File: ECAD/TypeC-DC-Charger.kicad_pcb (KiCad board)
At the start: 2 copper layers, 3 parts, among them U1 LM5175RHF, U2 TPS25741

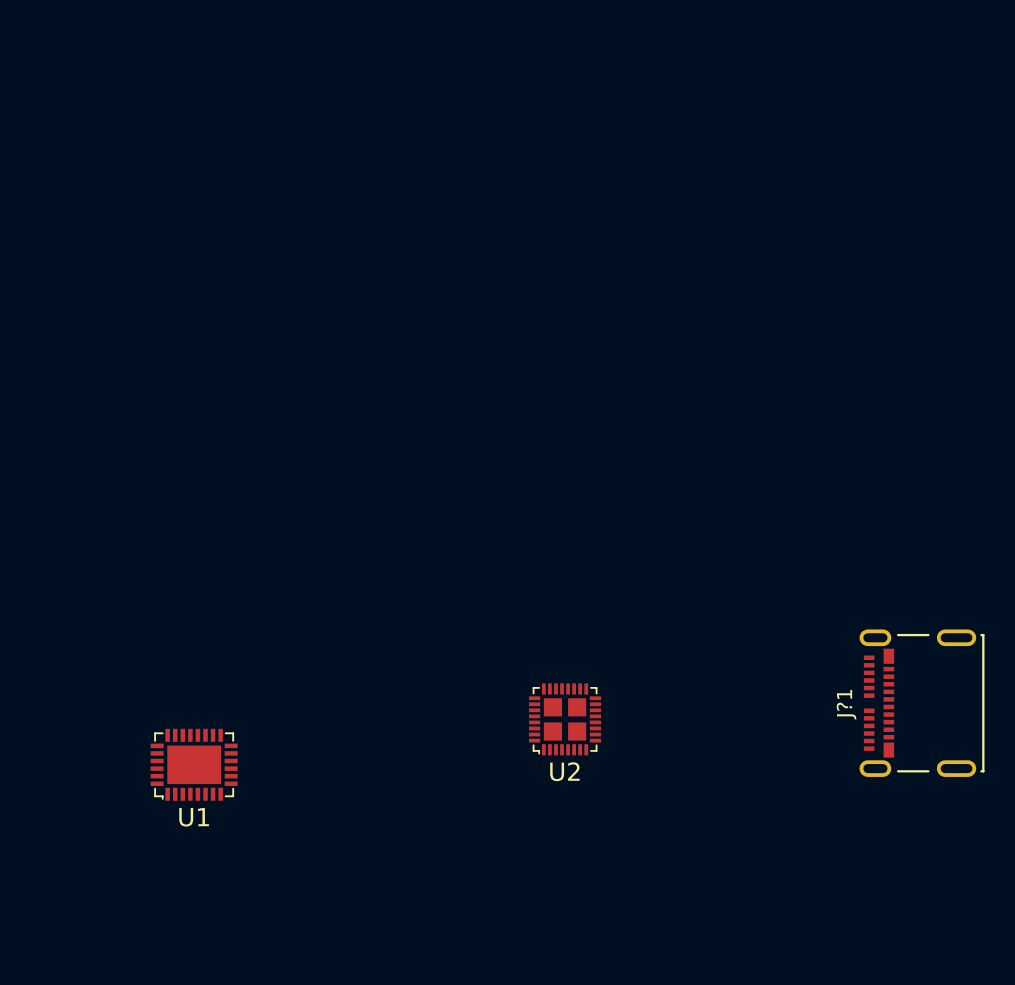
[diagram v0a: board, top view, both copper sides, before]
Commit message: Soft start circuit, Switched BC1.2 IC, more 0402 parts now, placement and routing.
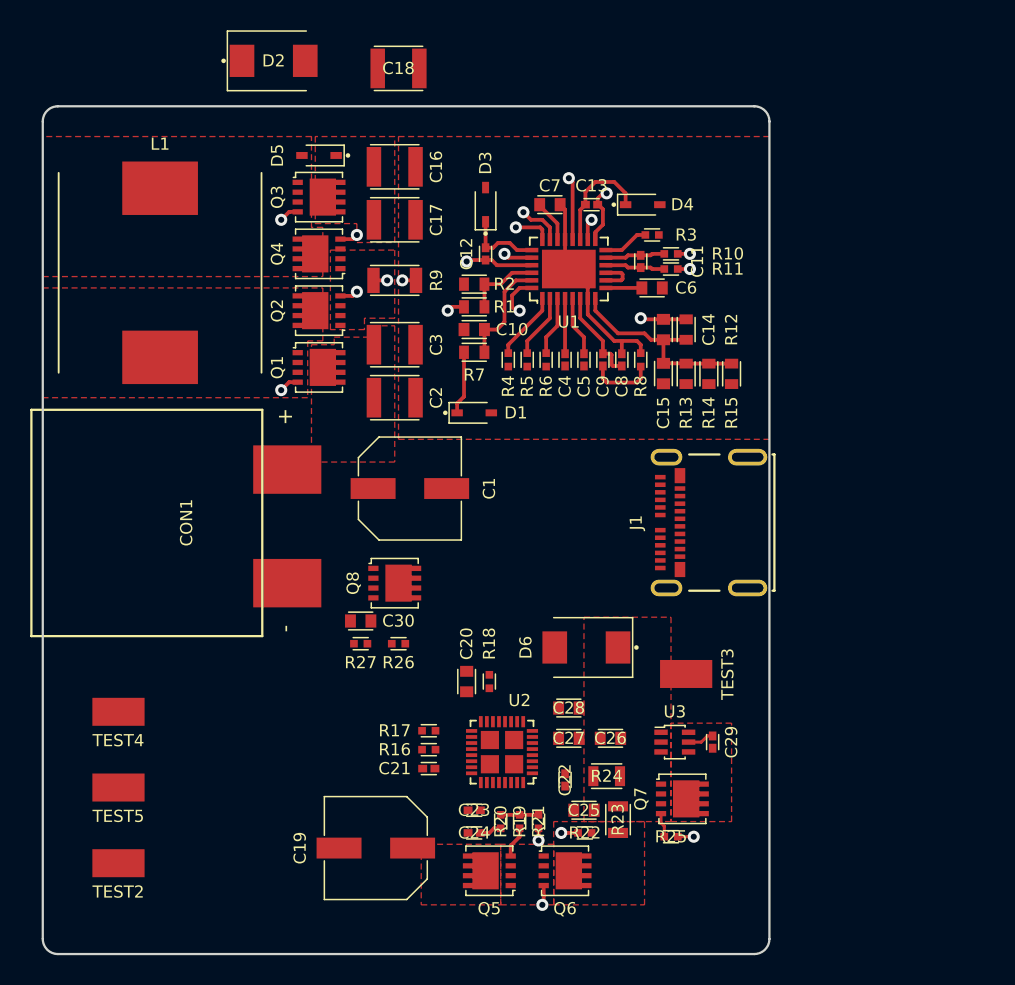
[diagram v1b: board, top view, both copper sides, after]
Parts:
- removed J?1: USB_C_SOCKET_RA_SMD, Applidyne_USB:MOLEX-105450-0101
- added C1: 100UF_ELEC_35V_660X580M, Applidyne_Capacitor:CAPAE660X580DD180L260L, F.Cu at (124.2, 75.2)
- added C10: 100NF_X7R_1608M, Applidyne_Capacitor:CAPC1608X90L, F.Cu at (128.5, 64.8)
- added C11: 47PF_X7R_1005M, Applidyne_Capacitor:CAPC1005X60L, F.Cu at (139.5, 60.2)
- added C12: 100NF_X7R_1005M, Applidyne_Capacitor:CAPC1005X60L, F.Cu at (129.2, 59.8)
- added C13: 100NF_X7R_1005M, Applidyne_Capacitor:CAPC1005X60L, F.Cu at (136.2, 56.5)
- added C14: 22NF_X7R_1608M, Applidyne_Capacitor:CAPC1608X90L, F.Cu at (141.0, 64.8)
- added C15: 100NF_X7R_1608M, Applidyne_Capacitor:CAPC1608X90L, F.Cu at (141.0, 67.7)
- added C16: 22UF_X7R_3225M, Applidyne_Capacitor:CAPC3225X170L, F.Cu at (123.2, 54.0)
- added C17: 22UF_X7R_3225M, Applidyne_Capacitor:CAPC3225X170L, F.Cu at (123.2, 57.5)
- added C18: 22UF_X7R_3225M, Applidyne_Capacitor:CAPC3225X170L, F.Cu at (123.5, 47.5)
- added C19: 100UF_ELEC_35V_660X580M, Applidyne_Capacitor:CAPAE660X580DD180L260L, F.Cu at (122.0, 99.0)
- added C2: 10UF_X7S_3225M, Applidyne_Capacitor:CAPC3225X170L, F.Cu at (123.2, 69.2)
- added C20: 330NF_X7R_1608M, Applidyne_Capacitor:CAPC1608X90L, F.Cu at (128.0, 88.0)
- added C21: 100NF_X7R_1005M, Applidyne_Capacitor:CAPC1005X60L, F.Cu at (125.5, 93.8)
- added C22: 100NF_X7R_1005M, Applidyne_Capacitor:CAPC1005X60L, F.Cu at (134.5, 94.5)
- added C23: 100NF_X7R_1005M, Applidyne_Capacitor:CAPC1005X60L, F.Cu at (128.5, 96.5)
- added C24: 10NF_X7R_1005M, Applidyne_Capacitor:CAPC1005X60L, F.Cu at (128.5, 98.0)
- added C25: 330NF_X7R_1608M, Applidyne_Capacitor:CAPC1608X90L, F.Cu at (135.8, 96.5)
- added C26: 6.8UF_X7R_1608M, Applidyne_Capacitor:CAPC1608X90L, F.Cu at (137.5, 91.8)
- added C27: 330PF_X7R_1608M, Applidyne_Capacitor:CAPC1608X90L, F.Cu at (134.8, 91.8)
- added C28: 330PF_X7R_1608M, Applidyne_Capacitor:CAPC1608X90L, F.Cu at (134.8, 89.8)
- added C29: 100NF_X7R_1005M, Applidyne_Capacitor:CAPC1005X60L, F.Cu at (144.2, 92.0)
- added C3: 10UF_X7S_3225M, Applidyne_Capacitor:CAPC3225X170L, F.Cu at (123.2, 65.8)
- added C30: 1UF_X7R_1608M, Applidyne_Capacitor:CAPC1608X90L, F.Cu at (121.0, 84.0)
- added C4: 100PF_C0G_1005M, Applidyne_Capacitor:CAPC1005X60L, F.Cu at (134.5, 66.8)
- added C5: 100NF_X7R_1005M, Applidyne_Capacitor:CAPC1005X60L, F.Cu at (135.8, 66.8)
- added C6: 1UF_X7R_1608M, Applidyne_Capacitor:CAPC1608X90L, F.Cu at (140.2, 62.0)
- added C7: 1UF_X7R_1608M, Applidyne_Capacitor:CAPC1608X90L, F.Cu at (133.5, 56.5)
- added C8: 100PF_C0G_1005M, Applidyne_Capacitor:CAPC1005X60L, F.Cu at (138.2, 66.8)
- added C9: 22NF_X7R_1005M, Applidyne_Capacitor:CAPC1005X60L, F.Cu at (137.0, 66.8)
- added CON1: XT60-PT-MALE, Applidyne_Connector:XT60-PT-MALE, F.Cu at (109.5, 77.5)
- added D1: 40V_500mA_SOD323, Applidyne_SOD:SOD2512X110L, F.Cu at (128.5, 70.2)
- added D2: CD214B-B250LF, Applidyne_SOD:SODFL5436X262L, F.Cu at (115.2, 47.0)
- added D3: 40V_500mA_SOD323, Applidyne_SOD:SOD2512X110L, F.Cu at (129.2, 56.5)
- added D4: 40V_500mA_SOD323, Applidyne_SOD:SOD2512X110L, F.Cu at (139.6, 56.5)
- added D5: 40V_500mA_SOD323, Applidyne_SOD:SOD2512X110L, F.Cu at (118.2, 53.2)
- added D6: SSB44-E3/52T_DO214AA, Applidyne_SOD:SODFL5436X262L, F.Cu at (135.9, 85.8)
- added J1: USB_C_SOCKET_RA_SMD, Applidyne_USB:MOLEX-105450-0101, F.Cu at (141.2, 77.5)
- added L1: 3.3uH_5050M, Applidyne_Inductor:INDM132129X500N, F.Cu at (107.8, 61.0)
- added Q1: CSD18543Q3A, Applidyne_SON:SON65P315X300X90-9T174X245L, F.Cu at (118.2, 67.2)
- added Q2: CSD18543Q3A, Applidyne_SON:SON65P315X300X90-9T174X245L, F.Cu at (118.2, 63.5)
- added Q3: CSD17551Q3A, Applidyne_SON:SON65P315X300X90-9T174X245L, F.Cu at (118.2, 56.0)
- added Q4: CSD17551Q3A, Applidyne_SON:SON65P315X300X90-9T174X245L, F.Cu at (118.2, 59.8)
- added Q5: CSD17579Q3A, Applidyne_SON:SON65P315X300X90-9T174X245L, F.Cu at (129.5, 100.5)
- added Q6: CSD17579Q3A, Applidyne_SON:SON65P315X300X90-9T174X245L, F.Cu at (134.5, 100.5)
- added Q7: CSD17579Q3A, Applidyne_SON:SON65P315X300X90-9T174X245L, F.Cu at (142.2, 95.8)
- added Q8: CSD18543Q3A, Applidyne_SON:SON65P315X300X90-9T174X245L, F.Cu at (123.2, 81.5)
- added R1: 249K_1608M, Applidyne_Resistor:RESC1608X50L, F.Cu at (128.5, 63.2)
- added R10: 100R_1005M, Applidyne_Resistor:RESC1005X40L, F.Cu at (141.5, 59.8)
- added R11: 100R_1005M, Applidyne_Resistor:RESC1005X40L, F.Cu at (141.5, 60.8)
- added R12: 49K9_1608M, Applidyne_Resistor:RESC1608X50L, F.Cu at (142.5, 64.8)
- added R13: 9K53_1608M, Applidyne_Resistor:RESC1608X50L, F.Cu at (142.5, 67.7)
- added R14: 4K99_1608M, Applidyne_Resistor:RESC1608X50L, F.Cu at (144.0, 67.7)
- added R15: 5K76_1608M, Applidyne_Resistor:RESC1608X50L, F.Cu at (145.5, 67.7)
- added R16: 1M_1005M, Applidyne_Resistor:RESC1005X40L, F.Cu at (125.5, 92.5)
- added R17: 680K_1005M, Applidyne_Resistor:RESC1005X40L, F.Cu at (125.5, 91.2)
- added R18: 100K_1005M, Applidyne_Resistor:RESC1005X40L, F.Cu at (129.5, 88.0)
- added R19: 10R_1005M, Applidyne_Resistor:RESC1005X40L, F.Cu at (131.5, 97.2)
- added R2: 41K2_1608M, Applidyne_Resistor:RESC1608X50L, F.Cu at (128.5, 61.8)
- added R20: 1K_1005M, Applidyne_Resistor:RESC1005X40L, F.Cu at (130.2, 97.2)
- added R21: 10R_1005M, Applidyne_Resistor:RESC1005X40L, F.Cu at (132.8, 97.2)
- added R22: 10R_1005M, Applidyne_Resistor:RESC1005X40L, F.Cu at (135.8, 98.0)
- added R23: 0.005R_2012M, Applidyne_Resistor:RESC2012X50L, F.Cu at (138.0, 97.1)
- added R24: 120R_2012M, Applidyne_Resistor:RESC2012X50L, F.Cu at (137.2, 94.2)
- added R25: 10R_1005M, Applidyne_Resistor:RESC1005X40L, F.Cu at (141.5, 98.2)
- added R26: 1M_1005M, Applidyne_Resistor:RESC1005X40L, F.Cu at (123.5, 85.5)
- added R27: 680K_1005M, Applidyne_Resistor:RESC1005X40L, F.Cu at (121.0, 85.5)
- added R3: 10K_1005M, Applidyne_Resistor:RESC1005X40L, F.Cu at (140.2, 58.5)
- added R4: 93K1_1005M, Applidyne_Resistor:RESC1005X40L, F.Cu at (130.8, 66.8)
- added R5: 0R_1005M, Applidyne_Resistor:RESC1005X40L, F.Cu at (132.0, 66.8)
- added R6: 84K5_1005M, Applidyne_Resistor:RESC1005X40L, F.Cu at (133.2, 66.8)
- added R7: 10R_1608M, Applidyne_Resistor:RESC1608X50L, F.Cu at (128.5, 66.2)
- added R8: 10K_1005M, Applidyne_Resistor:RESC1005X40L, F.Cu at (139.5, 66.8)
- added R9: 0.01R_3216M, Applidyne_Resistor:RESC3216X60L, F.Cu at (123.2, 61.5)
- added TEST2: PROBE_HOOK, Applidyne_Test:HARWIN_S1751-46, F.Cu at (105.0, 100.0)
- added TEST3: PROBE_HOOK, Applidyne_Test:HARWIN_S1751-46, F.Cu at (142.5, 87.5)
- added TEST4: PROBE_HOOK, Applidyne_Test:HARWIN_S1751-46, F.Cu at (105.0, 90.0)
- added TEST5: PROBE_HOOK, Applidyne_Test:HARWIN_S1751-46, F.Cu at (105.0, 95.0)
- added U3: TPS2514, Applidyne_SOT:SOT23-6P65_210X100L36X22L, F.Cu at (141.8, 92.0)
- moved U1 41.1 mm to (134.8, 60.8)
- moved U2 4.69 mm to (130.3, 92.7), turned to 90 degrees
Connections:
- net Net-(U2-Pad14) renamed ~UFP
- net Net-(U2-Pad27) renamed GDPG
- U1 pad 11: Net-(U1-Pad11) -> Net-(U1-Pad10)
- U1 pad 15: Net-(U1-Pad15) -> SW2
- U1 pad 16: Net-(U1-Pad16) -> HDRV2
- U1 pad 18: Net-(U1-Pad18) -> LDRV2
- U1 pad 19: Net-(U1-Pad19) -> GND
- U1 pad 20: Net-(U1-Pad20) -> /Power Supply/VCC
- U1 pad 21: Net-(U1-Pad21) -> VARIABLE_DC
- U1 pad 22: Net-(U1-Pad22) -> LDRV1
- U1 pad 24: Net-(U1-Pad24) -> HDRV1
- U1 pad 25: Net-(U1-Pad25) -> SW1
- U1 pad 28: Net-(U1-Pad28) -> VIN
- U1 pad 29: Net-(U1-Pad29) -> GND
- U1 pad 7: Net-(U1-Pad7) -> GND
- U1 pad 8: Net-(U1-Pad8) -> FB
- U1 pad 9: Net-(U1-Pad9) -> VARIABLE_DC
- U2 pad 10: Net-(U2-Pad10) -> /USBC Controller/DVDD
- U2 pad 17: Net-(U2-Pad17) -> /USBC Controller/DVDD
- U2 pad 18: Net-(U2-Pad18) -> /USBC Controller/DVDD
- U2 pad 19: Net-(U2-Pad19) -> /USBC Controller/DVDD
- U2 pad 2: Net-(U2-Pad2) -> CC1
- U2 pad 22: Net-(U2-Pad22) -> GND
- U2 pad 23: Net-(U2-Pad23) -> GND
- U2 pad 24: Net-(U2-Pad24) -> ISNS
- U2 pad 25: Net-(U2-Pad25) -> VARIABLE_DC
- U2 pad 26: Net-(U2-Pad26) -> VBUS
- U2 pad 29: Net-(U2-Pad29) -> GDNG
- U2 pad 3: Net-(U2-Pad3) -> GND
- U2 pad 30: Net-(U2-Pad30) -> GDNS
- U2 pad 31: Net-(U2-Pad31) -> DSCG
- U2 pad 32: Net-(U2-Pad32) -> G5V
- U2 pad 33: Net-(U2-Pad33) -> GND
- U2 pad 4: Net-(U2-Pad4) -> CC2
- U2 pad 5: Net-(U2-Pad5) -> GND
- U2 pad 6: Net-(U2-Pad6) -> /USBC Controller/DVDD
- U2 pad 7: Net-(U2-Pad7) -> CTRL1
- U2 pad 8: Net-(U2-Pad8) -> CTRL2
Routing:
- net GND: track 0.00 -> 15.4 mm, vias 0 -> 2
- net FB: track 0.00 -> 13.7 mm
- net VARIABLE_DC: track 0.00 -> 8.38 mm, vias 0 -> 2
- net Net-(C13-Pad1): track 0.00 -> 7.28 mm
- net Net-(C10-Pad2): track 0.00 -> 7.15 mm
- net Net-(C8-Pad1): track 0.00 -> 6.24 mm
- net LDRV2: track 0.00 -> 5.36 mm, vias 0 -> 2
- net Net-(C12-Pad1): track 0.00 -> 5.10 mm
- net Net-(R1-Pad2): track 0.00 -> 4.94 mm
- net Net-(R4-Pad1): track 0.00 -> 4.54 mm
- net SW1: track 0.00 -> 4.49 mm, vias 0 -> 1
- net Net-(C9-Pad2): track 0.00 -> 4.36 mm
- net Net-(R5-Pad1): track 0.00 -> 4.23 mm
- net Net-(D1-PadC): track 0.00 -> 4.19 mm
- net VIN: track 0.00 -> 4.04 mm, vias 0 -> 2
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- added copper zone on F.Cu, net /Connectors/5V
- added copper zone on F.Cu, net GDNS
- added copper zone on F.Cu, net GND
- added copper zone on In1.Cu, net GND
- added copper zone on F.Cu, net Net-(C25-Pad2)
- added copper zone on F.Cu, net RCS
- added copper zone on F.Cu, net SW1
- added copper zone on F.Cu, net SW2
- added copper zone on F.Cu, net VARIABLE_DC
- added copper zone on F.Cu, net VBUS
- added copper zone on F.Cu, net VIN
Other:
- board outline added: 48 x 56 mm
- copper layers 2 -> 4
- rule pad_to_mask_clearance: 0.2 -> 0.15

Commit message: Changed some parts to 0402, routing and pour improvements
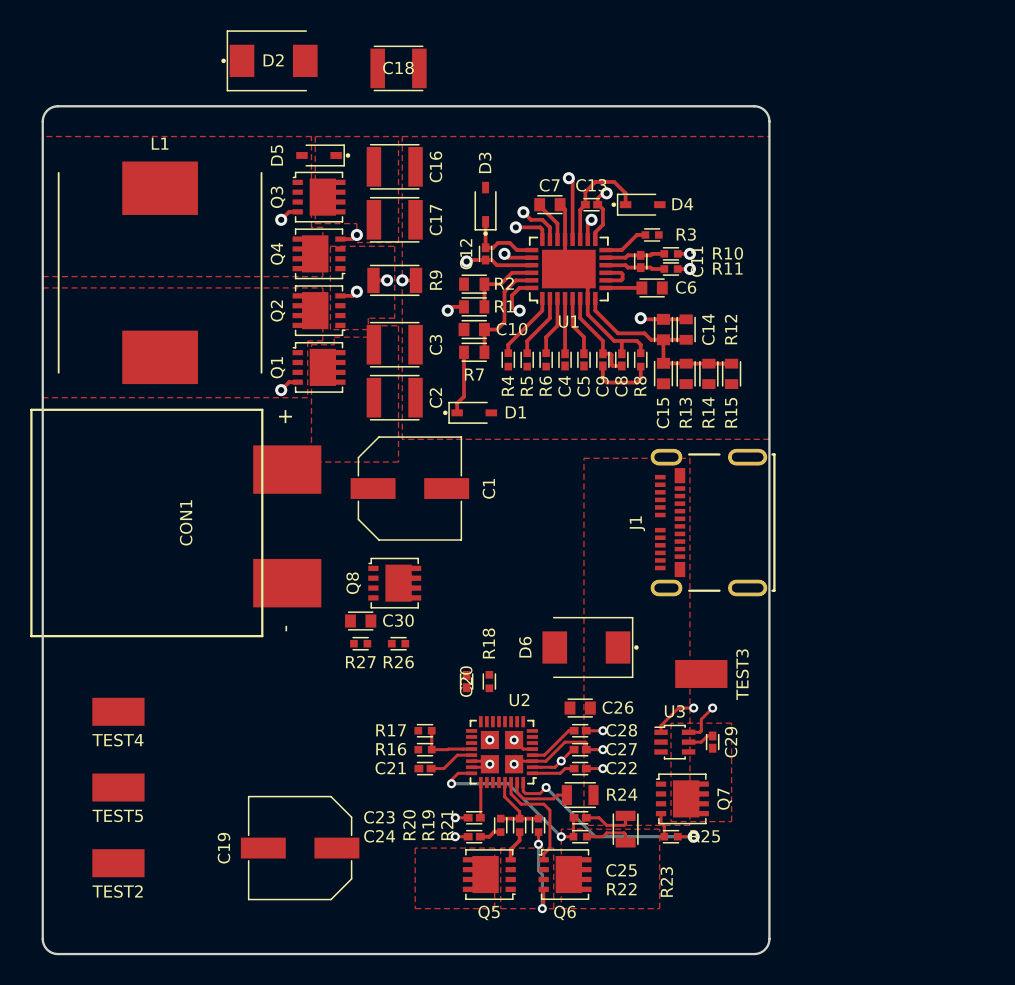
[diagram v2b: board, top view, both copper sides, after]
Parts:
- C20, C25: value 330NF_X7R_1608M -> 330NF_X5R_1005M; footprint Applidyne_Capacitor:CAPC1608X90L -> Applidyne_Capacitor:CAPC1005X60L
- C27, C28: value 330PF_X7R_1608M -> 330PF_X7R_1005M; footprint Applidyne_Capacitor:CAPC1608X90L -> Applidyne_Capacitor:CAPC1005X60L
- moved C19 5.00 mm to (117.0, 99.0)
- moved C26 2.83 mm to (135.5, 89.8)
- moved R24 2.15 mm to (135.5, 95.5)
- moved C28 1.68 mm to (135.5, 91.2), turned to 0 degrees
- moved C22 1.25 mm to (135.5, 93.8), turned to 0 degrees
- moved C27 1.06 mm to (135.5, 92.5)
- moved TEST3 1.00 mm to (143.5, 87.5)
- moved R23 0.80 mm to (138.5, 97.8)
- moved C25 0.56 mm to (135.5, 97.0), turned to 0 degrees
- moved C23 0.50 mm to (128.5, 97.0)
- moved R22 0.39 mm to (135.5, 98.2)
- moved C21 0.25 mm to (125.2, 93.8)
- moved C24 0.25 mm to (128.5, 98.2)
- moved Q5 0.25 mm to (129.5, 100.8)
- moved Q6 0.25 mm to (134.5, 100.8)
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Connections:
- C25 pad 1: VBUS -> ISNS
- C25 pad 2: Net-(C25-Pad2) -> VBUS
- C27 pad 1: GND -> CC1
- C27 pad 2: CC1 -> GND
- C28 pad 1: GND -> CC2
- C28 pad 2: CC2 -> GND
- Q6 pad 3: Net-(C25-Pad2) -> Net-(Q6-Pad3)
- R22 pad 1: Net-(C25-Pad2) -> Net-(Q6-Pad3)
- R23 pad 2: Net-(C25-Pad2) -> Net-(Q6-Pad3)
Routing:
- net GND: track 15.4 -> 30.3 mm, vias 2 -> 11
- net G5V: track 1.06 -> 14.5 mm, vias 1 -> 2
- net ISNS: track 1.11 -> 12.5 mm, vias 1 -> 2
- net GDNS: track 0.00 -> 7.21 mm
- net Net-(Q6-Pad1): track 2.12 -> 6.47 mm
- net DSCG: track 0.00 -> 4.22 mm
- net Net-(R16-Pad2): track 0.00 -> 3.90 mm
- net CC2: track 0.00 -> 3.42 mm
- net VBUS: track 0.00 -> 3.38 mm
- net Net-(Q6-Pad3): track 0.00 -> 3.23 mm
- net CC1: track 0.00 -> 3.23 mm, vias 0 -> 1
- net D+: track 0.00 -> 3.08 mm, vias 0 -> 1
- net Net-(C21-Pad1): track 0.00 -> 3.04 mm
- net Net-(C22-Pad1): track 0.00 -> 2.88 mm
- net GDNG: track 2.50 -> 5.30 mm
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- added copper zone on F.Cu, net Net-(Q6-Pad3)
- removed copper zone on F.Cu, net Net-(C25-Pad2)
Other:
- net class TPS25741 added: clearance 0.15, trace_width 0.22, via_dia 0.6, via_drill 0.35

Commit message: Added better input protection with soft start, over voltage protection, cap discharge etc. Fixed some part selections, reformatting in schematic. Placement of input protection circuit. Cleanup of PCB layout.
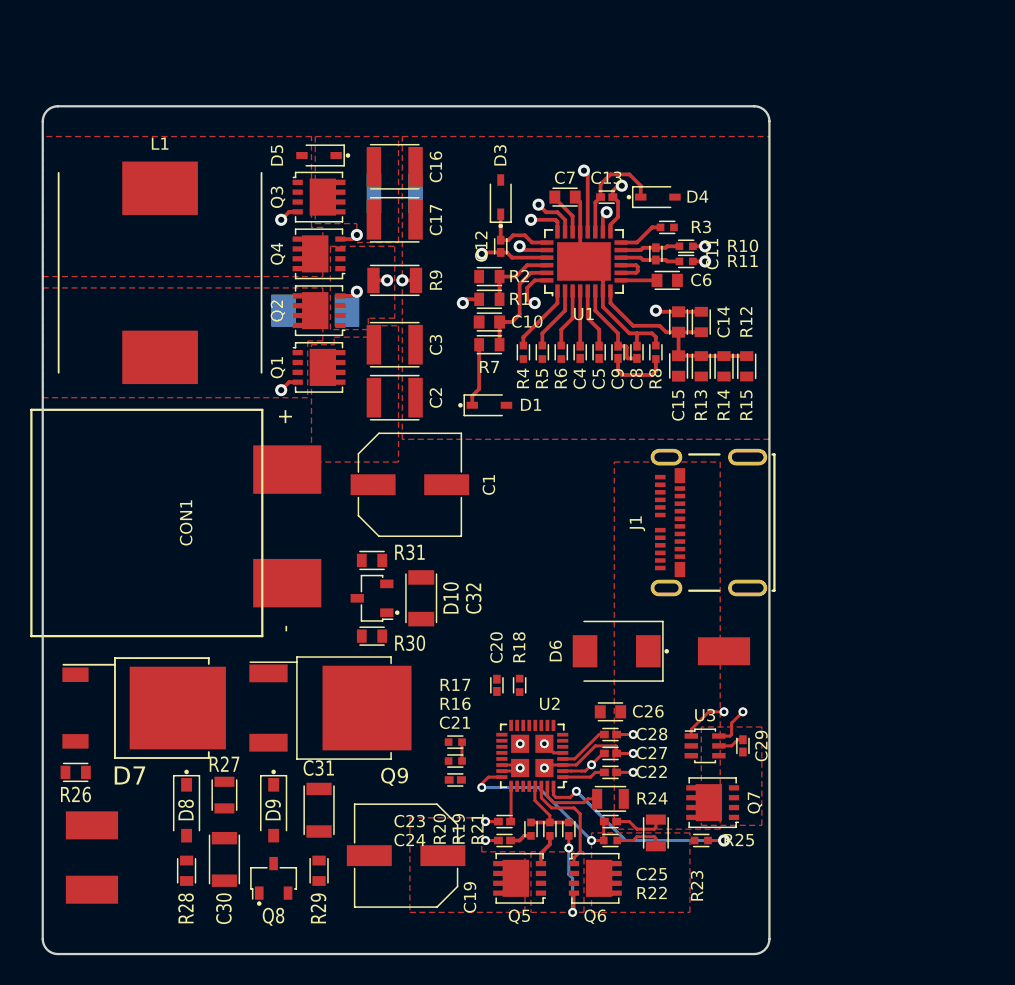
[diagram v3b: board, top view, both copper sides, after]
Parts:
- removed TEST4: PROBE_HOOK, Applidyne_Test:HARWIN_S1751-46
- added C31: 1UF_X7R_3216M, Applidyne_Resistor:RESC3216X60L, F.Cu at (118.2, 96.5)
- added C32: 100NF_X7R_3216M, Applidyne_Capacitor:CAPC3216X135L, F.Cu at (125.0, 82.5)
- added D10: BAV99, Applidyne_SOT:SOT95P240X110-3L16L, F.Cu at (121.8, 82.5)
- added D7: 300V_10A_DPAK, Applidyne_DPAK:TO440P972X240-3N, F.Cu at (106.7, 89.8)
- added D8: 33V_500mW_SOD123, Applidyne_SOD:SOD3715X145L, F.Cu at (109.5, 96.5)
- added D9: 33V_500mW_SOD123, Applidyne_SOD:SOD3715X145L, F.Cu at (115.2, 96.5)
- added Q9: IRFR9024NTRPBF, Applidyne_DPAK:DPAK4P229_990X239L159X95L, F.Cu at (119.0, 89.8)
- added R28: 22K_1608M, Applidyne_Resistor:RESC1608X50L, F.Cu at (109.5, 100.5)
- added R29: 332K_1608M, Applidyne_Resistor:RESC1608X50L, F.Cu at (118.2, 100.5)
- added R30: 10R_1608M, Applidyne_Resistor:RESC1608X50L, F.Cu at (121.8, 85.0)
- added R31: 10K0_1608M, Applidyne_Resistor:RESC1608X50L, F.Cu at (121.8, 80.0)
- C18, D2: moved to B.Cu
- C30: value 1UF_X7R_1608M -> 1UF_X7R_3216M; footprint Applidyne_Capacitor:CAPC1608X90L -> Applidyne_Resistor:RESC3216X60L
- Q8: value CSD18543Q3A -> BC857B; footprint Applidyne_SON:SON65P315X300X90-9T174X245L -> Applidyne_SOT:SOT95P240X110-3L16L
- R26: value 1M_1005M -> 100K_1608M; footprint Applidyne_Resistor:RESC1005X40L -> Applidyne_Resistor:RESC1608X50L
- R27: value 680K_1005M -> 10R_2012M; footprint Applidyne_Resistor:RESC1005X40L -> Applidyne_Resistor:RESC2012X50L
- moved R26 23.0 mm to (102.2, 94.0)
- moved Q8 21.1 mm to (115.2, 101.0), turned to 0 degrees
- moved C30 18.1 mm to (112.0, 99.8), turned to 270 degrees
- moved D2 16.7 mm to (118.0, 63.5)
- moved R27 13.5 mm to (112.0, 95.5), turned to 270 degrees
- moved C18 8.25 mm to (123.2, 55.8)
- moved C19 7.02 mm to (124.0, 99.5)
- moved TEST5 3.05 mm to (103.2, 97.5)
- moved TEST2 2.47 mm to (103.2, 101.8)
- moved C21 2.14 mm to (127.2, 94.5)
- moved R16 2.14 mm to (127.2, 93.2)
- moved R17 2.14 mm to (127.2, 92.0)
- moved TEST3 2.12 mm to (145.0, 86.0)
- moved C20 2.02 mm to (130.0, 88.2)
- moved C22 2.02 mm to (137.5, 94.0)
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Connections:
- C30 pad 2: Net-(C30-Pad2) -> GND
- CON1 pad 1: Net-(C30-Pad2) -> GND
- CON1 pad 2: VIN -> Net-(CON1-Pad2)
- Q7 pad 2: VBUS -> /Connectors/5V
- Q7 pad 3: /Connectors/5V -> VBUS
- Q8 pad 1: Net-(C30-Pad1) -> Net-(D8-PadC)
- Q8 pad 2: Net-(C30-Pad2) -> Net-(C31-Pad1)
- Q8 pad 3: GND -> Net-(C31-Pad2)
- R26 pad 1: VIN -> Net-(D8-PadC)
- R26 pad 2: Net-(C30-Pad1) -> Net-(CON1-Pad2)
- R27 pad 1: Net-(C30-Pad1) -> Net-(C31-Pad1)
- R27 pad 2: Net-(C30-Pad2) -> Net-(C30-Pad1)
- TEST5 pad 1: Net-(C30-Pad2) -> GND
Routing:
- net Net-(C21-Pad1): track 3.04 -> 0.00 mm
- net Net-(R16-Pad2): track 3.90 -> 1.25 mm
- net Net-(Q7-Pad1): track 1.61 -> 0.00 mm
